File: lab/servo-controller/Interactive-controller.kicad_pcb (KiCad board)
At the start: 2 copper layers, 90 x 80 mm, 6 parts, among them U1 atmega328p

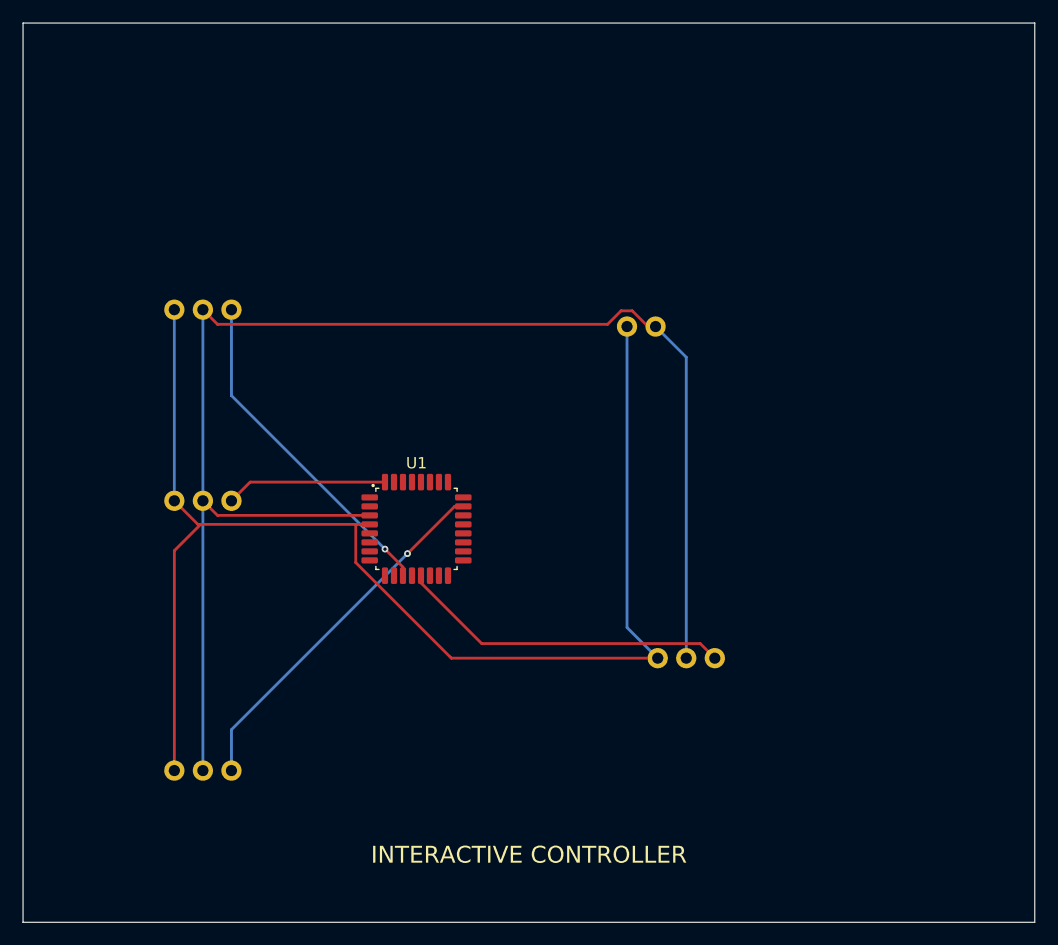
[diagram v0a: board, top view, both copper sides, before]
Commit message: lab: every board is a real board: an Arduino Nano and registry parts, routed, ready to order
The lab boards ran on simulation-only envelopes (labMcu, labDisplay, a battery). Now each is
an Arduino Nano on two sockets on the back (flashed over its USB, the image the app builds),
its lights LEDs through 1 kΩ, its knobs PTV09A pots, its display the MAX7219 eight-digit
module, its sensors an SHT31 and an SCD40 with their datasheets' support circuits, the FTDI
header for the serial console; the servo boards take 5 V on a screw terminal with a bulk
capacitor. All ten check complete with no errors or warnings, their firmware unchanged
(serial-device now on the 328P), and run in the lab without a fault (3 s each, dev host).

The registry: every interactive board must be ready to order and flash (publish.mjs refuses
one that is not; status simulation-only removed).

Claude-Session: https://claude.ai/code/session_01ATmMmxyrWxFwR3nTdXUrcx
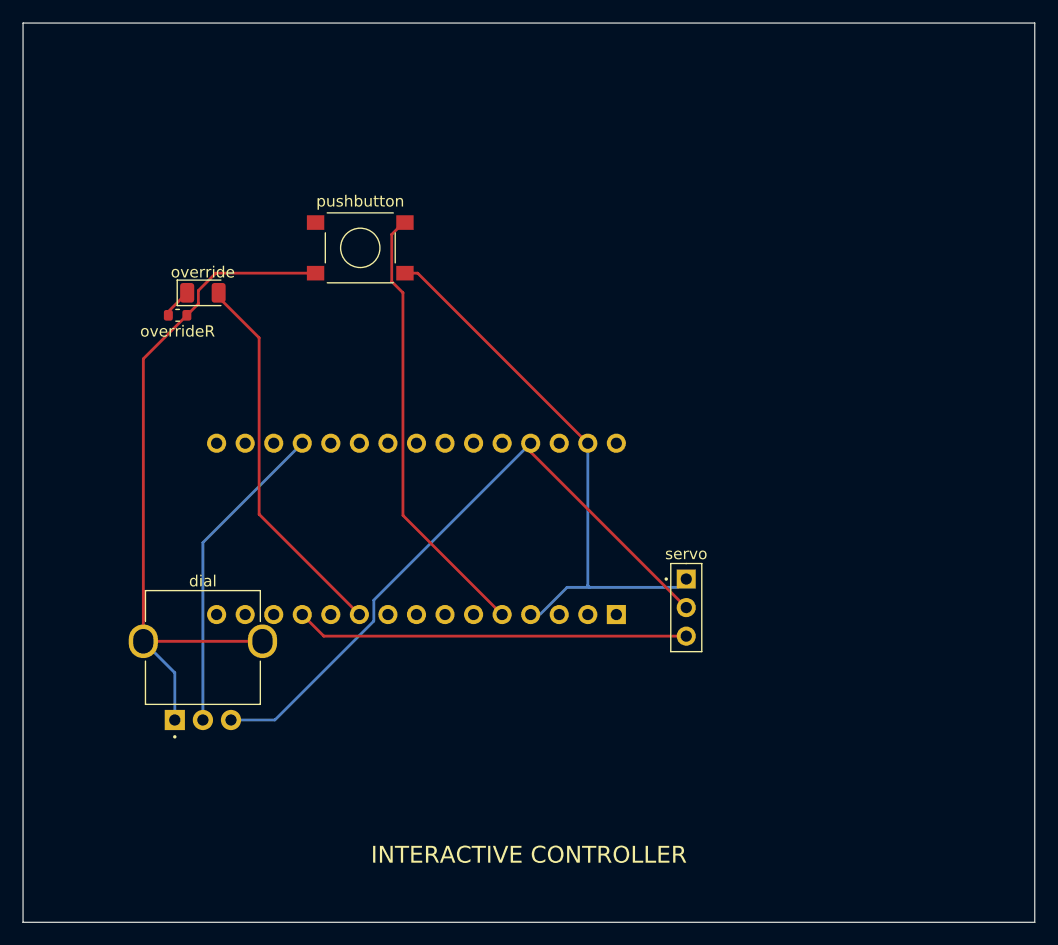
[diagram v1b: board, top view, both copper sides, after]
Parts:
- removed battery: battery, Regulated battery module
- removed button: button, Button module
- removed knob: potentiometer, Potentiometer module
- removed the override at (116.0, 144.0)
- removed the servo at (159.0, 172.0)
- added dial: PTV09A-4020F-B103, Potentiometer_Bourns_PTV09A-4_Vertical, F.Cu at (116.0, 182.0)
- added override: green, LED_1206_3216Metric, F.Cu at (116.0, 144.0)
- added overrideR: 1kohm, R_0603_1608Metric, F.Cu at (113.8, 146.0)
- added pushbutton: PTS645SM43SMTR92 LFS, SW_Tactile_SPST_6x6mm_SMD, F.Cu at (130.0, 140.0)
- added servo: RC servo header, 1 x 3 pins, 2.54 mm, PinHeader_1x03_P2.54mm_Vertical, F.Cu at (159.0, 172.0)
- U1: value atmega328p -> A000005; footprint TQFP-32_7x7mm_P0.8mm -> Arduino_Nano_Socket_2x15_P2.54mm_W15.24mm; moved to B.Cu
- turned U1 to 90 degrees
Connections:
- U1 pad 10: (no net) -> OVERRIDE
- U1 pad 11: OVERRIDE -> (no net)
- U1 pad 12: (no net) -> SERVO
- U1 pad 13: SERVO -> (no net)
- U1 pad 19: (no net) -> ANALOG
- U1 pad 23: ANALOG -> (no net)
- U1 pad 27: (no net) -> V5
- U1 pad 29: (no net) -> GND
- U1 pad 3: GND -> (no net)
- U1 pad 4: V5 -> GND
- U1 pad 5: (no net) -> BUTTON
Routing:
- net V5: track 122.5 -> 58.3 mm
- net BUTTON: track 14.3 -> 39.5 mm
- net GND: track 128.9 -> 111.7 mm
- net SERVO: track 29.6 -> 35.0 mm
- net ANALOG: track 32.5 -> 28.3 mm, vias 1 -> 0
- net OVERRIDE: track 30.0 -> 33.8 mm, vias 1 -> 0
- net OVERRIDE_K: track 0.00 -> 2.69 mm

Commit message: Boards pass check and KiCad 10's DRC again: holes in courtyards, the USB net rename
pcbkit's check now has KiCad 10's pth/npth_inside_courtyard (pcbkit be5b6955), and 13 boards
failed it. KiCad's own DRC (kicad-cli 10) reports the same holes on every one of them.

- Parts that really stand above the holes under them (a screen or a Nano on its sockets, the
  Delta-S02's КМ-6 capacitors flat under its chips, as the factory placed them): a courtyard rule
  for the pair, written to each board's .kicad_dru, so KiCad's DRC agrees.
- Real collisions moved: servo-controller's dial 3 mm up (the Nano's socket pins came out under
  it), c3-pocket's fourth M3 hole from under a cell holder to the top edge's middle, s3-rgb's
  D-pad 2 mm up (a holder's peg came through under the down key).
- v003-emu, c3-pocket, rp2040-tft, rp2350-psram, s3-rgb, teensy41: re-routed for the standard USB
  block's renamed net (usb/raw is usb/vbusIn since pcbkit 2088839e): their tracks still carried
  the old name and shorted the fuse and connector pads.
- p4-touch-7: its board file still had a courtyard for the panel the design gives none (KiCad
  reported 114 courtyard errors); written again.

Measured on the dev host: all 44 registry boards `pcbkit check` complete with 0 errors, and
kicad-cli pcb drc 0 errors on every board.

Claude-Session: https://claude.ai/code/session_018URVYF1YPgyrMNetY9yT1T
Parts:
- moved dial 3.00 mm to (116.0, 185.0)
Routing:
- net ANALOG: track 28.3 -> 31.3 mm
- net V5: track 58.3 -> 59.5 mm

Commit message: lab, examples, esp32-p4-touch-lcd-7b: the sweep's errors and stale parts
- lab/stopwatch: the display module stands on its socket above the Nano's socket pins. It now has
  the courtyard waiver the other Nano boards have (13 pth-inside-courtyard -> 0).
- lab/servo-controller: outline 90 x 80 -> 70 x 70 mm, with the parts where they were
  (board-oversized, plan-size: 11 % parts). Complete, 0 warnings.
- examples/blinker, examples/led-bar, devices/esp32-p4-touch-lcd-7b: `pcbkit parts` chose again
  where the recorded part no longer met the need (part-stale).

Claude-Session: https://claude.ai/code/session_01B3VRfBCg9vAvGVWujVGarr
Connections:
- pushbutton pad 2: BUTTON -> GND
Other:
- board size 90 x 80 mm -> 70 x 70 mm
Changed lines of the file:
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@@
   (footprint "Arduino_Nano_Socket_2x15_P2.54mm_W15.24mm" (layer "B.Cu") (at 135 165 90)
     (descr "Arduino Nano on two 1x15 female headers 15.24 mm apart, its USB end at +Y (Arduino's drawing): pins 1-15 the right row from the bottom (D1/TX … D12), 16-30 the left row from the top (D13 … VIN)")
-    (tags "THT module pin socket female header")
+    (tags "THT module pin header soldered")
     (property "Reference" "U1" (at 0 -24.05 90) (layer "B.SilkS") (effects (font (size 1 1) (thickness 0.15)) (justify mirror)))
     (property "Value" "A000005" (at 0 0 0) (layer "B.Fab") (hide yes) (effects (font (size 1 1))))
@@
     (property "Status" "checked" (at 0 0 0) (layer "B.Fab") (hide yes) (effects (font (size 1 1))))
     (property "pcbkit" "U1" (at 0 0 0) (layer "B.Fab") (hide yes) (effects (font (size 1 1))))
-    (fp_rect (start 9.25 21.85) (end -9.25 -23.35) (stroke (width 0.05) (type solid)) (layer "B.CrtYd"))
+    (fp_poly (pts (xy -6.12 19.28) (xy -9.12 19.28) (xy -9.12 16.28) (xy -6.12 16.28)) (stroke (width 0.05) (type solid)) (fill none) (layer "B.CrtYd"))
+    (fp_poly (pts (xy -6.12 16.74) (xy -9.12 16.74) (xy -9.12 13.74) (xy -6.12 13.74)) (stroke (width 0.05) (type solid)) (fill none) (layer "B.CrtYd"))
+    (fp_poly (pts (xy -6.12 14.2) (xy -9.12 14.2) (xy -9.12 11.2) (xy -6.12 11.2)) (stroke (width 0.05) (type solid)) (fill none) (layer "B.CrtYd"))
+    (fp_poly (pts (xy -6.12 11.66) (xy -9.12 11.66) (xy -9.12 8.66) (xy -6.12 8.66)) (stroke (width 0.05) (type solid)) (fill none) (layer "B.CrtYd"))
+    (fp_poly (pts (xy -6.12 9.12) (xy -9.12 9.12) (xy -9.12 6.12) (xy -6.12 6.12)) (stroke (width 0.05) (type solid)) (fill none) (layer "B.CrtYd"))
+    (fp_poly (pts (xy -6.12 6.58) (xy -9.12 6.58) (xy -9.12 3.58) (xy -6.12 3.58)) (stroke (width 0.05) (type solid)) (fill none) (layer "B.CrtYd"))
+    (fp_poly (pts (xy -6.12 4.04) (xy -9.12 4.04) (xy -9.12 1.04) (xy -6.12 1.04)) (stroke (width 0.05) (type solid)) (fill none) (layer "B.CrtYd"))
+    (fp_poly (pts (xy -6.12 1.5) (xy -9.12 1.5) (xy -9.12 -1.5) (xy -6.12 -1.5)) (stroke (width 0.05) (type solid)) (fill none) (layer "B.CrtYd"))
+    (fp_poly (pts (xy -6.12 -1.04) (xy -9.12 -1.04) (xy -9.12 -4.04) (xy -6.12 -4.04)) (stroke (width 0.05) (type solid)) (fill none) (layer "B.CrtYd"))
+    (fp_poly (pts (xy -6.12 -3.58) (xy -9.12 -3.58) (xy -9.12 -6.58) (xy -6.12 -6.58)) (stroke (width 0.05) (type solid)) (fill none) (layer "B.CrtYd"))
+    (fp_poly (pts (xy -6.12 -6.12) (xy -9.12 -6.12) (xy -9.12 -9.12) (xy -6.12 -9.12)) (stroke (width 0.05) (type solid)) (fill none) (layer "B.CrtYd"))
+    (fp_poly (pts (xy -6.12 -8.66) (xy -9.12 -8.66) (xy -9.12 -11.66) (xy -6.12 -11.66)) (stroke (width 0.05) (type solid)) (fill none) (layer "B.CrtYd"))
+    (fp_poly (pts (xy -6.12 -11.2) (xy -9.12 -11.2) (xy -9.12 -14.2) (xy -6.12 -14.2)) (stroke (width 0.05) (type solid)) (fill none) (layer "B.CrtYd"))
+    (fp_poly (pts (xy -6.12 -13.74) (xy -9.12 -13.74) (xy -9.12 -16.74) (xy -6.12 -16.74)) (stroke (width 0.05) (type solid)) (fill none) (layer "B.CrtYd"))
+    (fp_poly (pts (xy -6.12 -16.28) (xy -9.12 -16.28) (xy -9.12 -19.28) (xy -6.12 -19.28)) (stroke (width 0.05) (type solid)) (fill none) (layer "B.CrtYd"))
+    (fp_poly (pts (xy 9.12 -16.28) (xy 6.12 -16.28) (xy 6.12 -19.28) (xy 9.12 -19.28)) (stroke (width 0.05) (type solid)) (fill none) (layer "B.CrtYd"))
+    (fp_poly (pts (xy 9.12 -13.74) (xy 6.12 -13.74) (xy 6.12 -16.74) (xy 9.12 -16.74)) (stroke (width 0.05) (type solid)) (fill none) (layer "B.CrtYd"))
+    (fp_poly (pts (xy 9.12 -11.2) (xy 6.12 -11.2) (xy 6.12 -14.2) (xy 9.12 -14.2)) (stroke (width 0.05) (type solid)) (fill none) (layer "B.CrtYd"))
+    (fp_poly (pts (xy 9.12 -8.66) (xy 6.12 -8.66) (xy 6.12 -11.66) (xy 9.12 -11.66)) (stroke (width 0.05) (type solid)) (fill none) (layer "B.CrtYd"))
+    (fp_poly (pts (xy 9.12 -6.12) (xy 6.12 -6.12) (xy 6.12 -9.12) (xy 9.12 -9.12)) (stroke (width 0.05) (type solid)) (fill none) (layer "B.CrtYd"))
+    (fp_poly (pts (xy 9.12 -3.58) (xy 6.12 -3.58) (xy 6.12 -6.58) (xy 9.12 -6.58)) (stroke (width 0.05) (type solid)) (fill none) (layer "B.CrtYd"))
+    (fp_poly (pts (xy 9.12 -1.04) (xy 6.12 -1.04) (xy 6.12 -4.04) (xy 9.12 -4.04)) (stroke (width 0.05) (type solid)) (fill none) (layer "B.CrtYd"))
+    (fp_poly (pts (xy 9.12 1.5) (xy 6.12 1.5) (xy 6.12 -1.5) (xy 9.12 -1.5)) (stroke (width 0.05) (type solid)) (fill none) (layer "B.CrtYd"))
+    (fp_poly (pts (xy 9.12 4.04) (xy 6.12 4.04) (xy 6.12 1.04) (xy 9.12 1.04)) (stroke (width 0.05) (type solid)) (fill none) (layer "B.CrtYd"))
+    (fp_poly (pts (xy 9.12 6.58) (xy 6.12 6.58) (xy 6.12 3.58) (xy 9.12 3.58)) (stroke (width 0.05) (type solid)) (fill none) (layer "B.CrtYd"))
+    (fp_poly (pts (xy 9.12 9.12) (xy 6.12 9.12) (xy 6.12 6.12) (xy 9.12 6.12)) (stroke (width 0.05) (type solid)) (fill none) (layer "B.CrtYd"))
+    (fp_poly (pts (xy 9.12 11.66) (xy 6.12 11.66) (xy 6.12 8.66) (xy 9.12 8.66)) (stroke (width 0.05) (type solid)) (fill none) (layer "B.CrtYd"))
+    (fp_poly (pts (xy 9.12 14.2) (xy 6.12 14.2) (xy 6.12 11.2) (xy 9.12 11.2)) (stroke (width 0.05) (type solid)) (fill none) (layer "B.CrtYd"))
+    (fp_poly (pts (xy 9.12 16.74) (xy 6.12 16.74) (xy 6.12 13.74) (xy 9.12 13.74)) (stroke (width 0.05) (type solid)) (fill none) (layer "B.CrtYd"))
+    (fp_poly (pts (xy 9.12 19.28) (xy 6.12 19.28) (xy 6.12 16.28) (xy 9.12 16.28)) (stroke (width 0.05) (type solid)) (fill none) (layer "B.CrtYd"))
+    (fp_poly (pts (xy 6.2 17.29) (xy -5.515 17.29) (xy -5.515 -10.35) (xy 6.2 -10.35)) (stroke (width 0.05) (type solid)) (fill none) (layer "B.CrtYd"))
     (fp_line (start 0 -23.21) (end 9.11 -23.21) (stroke (width 0.12) (type solid)) (layer "B.SilkS"))
     (fp_line (start 9.11 -23.21) (end 9.11 21.71) (stroke (width 0.12) (type solid)) (layer "B.SilkS"))
@@
   )
   (footprint "SW_Tactile_SPST_6x6mm_SMD" (layer "F.Cu") (at 130 140 0)
-    (descr "Tactile switch, 6 x 6 x 4.3 mm, SMD, 4 pads (1-2 and 3-4 joined)")
+    (descr "Tactile switch, 6 x 6 x 4.3 mm, SMD, 4 pads, 2 to each contact")
     (tags "switch tactile button 6x6")
     (property "Reference" "pushbutton" (at 0 -4.141667 0) (layer "F.SilkS") (effects (font (size 1 1) (thickness 0.15))))
@@
     (property "Manufacturer" "C&K" (at 0 0 0) (layer "F.Fab") (hide yes) (effects (font (size 1 1))))
     (property "pcbkit" "pushbutton" (at 0 0 0) (layer "F.Fab") (hide yes) (effects (font (size 1 1))))
-    (jumper_pad_groups ("1" "2") ("3" "4"))
+    (duplicate_pad_numbers_are_jumpers yes)
     (fp_rect (start -5 3.25) (end 5 -3.25) (stroke (width 0.05) (type solid)) (layer "F.CrtYd"))
     (fp_line (start -3.11 -1.34) (end -3.11 1.34) (stroke (width 0.12) (type solid)) (layer "F.SilkS"))
@@
     (fp_circle (center 0 0) (end 1.75 0) (stroke (width 0.12) (type solid)) (fill none) (layer "F.SilkS"))
     (pad "1" smd rect (at -3.975 -2.25 0) (size 1.55 1.3) (layers "F.Cu" "F.Paste" "F.Mask") (solder_mask_margin 0.05) (net 2 "BUTTON"))
-    (pad "2" smd rect (at 3.975 -2.25 0) (size 1.55 1.3) (layers "F.Cu" "F.Paste" "F.Mask") (solder_mask_margin 0.05) (net 2 "BUTTON"))
-    (pad "3" smd rect (at -3.975 2.25 0) (size 1.55 1.3) (layers "F.Cu" "F.Paste" "F.Mask") (solder_mask_margin 0.05) (net 3 "GND"))
-    (pad "4" smd rect (at 3.975 2.25 0) (size 1.55 1.3) (layers "F.Cu" "F.Paste" "F.Mask") (solder_mask_margin 0.05) (net 3 "GND"))
+    (pad "1" smd rect (at 3.975 -2.25 0) (size 1.55 1.3) (layers "F.Cu" "F.Paste" "F.Mask") (solder_mask_margin 0.05) (net 2 "BUTTON"))
+    (pad "2" smd rect (at -3.975 2.25 0) (size 1.55 1.3) (layers "F.Cu" "F.Paste" "F.Mask") (solder_mask_margin 0.05) (net 3 "GND"))
+    (pad "2" smd rect (at 3.975 2.25 0) (size 1.55 1.3) (layers "F.Cu" "F.Paste" "F.Mask") (solder_mask_margin 0.05) (net 3 "GND"))
   )
   (footprint "PinHeader_1x03_P2.54mm_Vertical" (layer "F.Cu") (at 159 172 0)
@@
     (pad "3" thru_hole oval (at 0 2.54 0) (size 1.7 1.7) (drill 1) (layers "*.Cu" "*.Mask") (solder_mask_margin 0.05) (net 6 "SERVO"))
   )
-  (gr_text "INTERACTIVE CONTROLLER" (at 145 194 0) (layer "F.SilkS") (effects (font (size 1.5 1.5) (thickness 0.15))))
-  (group "pcbkit" (members "e2fbeeec-4a09-db61-f9d1-26c3135e6155"))
   (segment (start 114.6 144) (end 112.925 145.675) (width 0.25) (layer "F.Cu") (net 5))
   (segment (start 112.925 145.675) (end 112.925 146) (width 0.25) (layer "F.Cu") (net 5))
@@
   (segment (start 133.85 137.75) (end 133.975 137.75) (width 0.25) (layer "F.Cu") (net 2))
   (segment (start 121.3 178) (end 110.7 178) (width 0.25) (layer "F.Cu") (net 3))
-  (gr_line (start 100 200) (end 190 200) (stroke (width 0.1) (type solid)) (layer "Edge.Cuts"))
-  (gr_line (start 190 200) (end 190 120) (stroke (width 0.1) (type solid)) (layer "Edge.Cuts"))
-  (gr_line (start 190 120) (end 100 120) (stroke (width 0.1) (type solid)) (layer "Edge.Cuts"))
-  (gr_line (start 100 120) (end 100 200) (stroke (width 0.1) (type solid)) (layer "Edge.Cuts"))
   (segment (start 145.16 157.38) (end 145.16 158.16) (width 0.25) (layer "F.Cu") (net 7))
   (segment (start 145.16 158.16) (end 159 172) (width 0.25) (layer "F.Cu") (net 7))
@@
   (segment (start 110.7 178) (end 113.5 180.8) (width 0.25) (layer "B.Cu") (net 3))
   (segment (start 113.5 180.8) (end 113.5 185) (width 0.25) (layer "B.Cu") (net 3))
+  (gr_text "INTERACTIVE CONTROLLER" (at 135 195 0) (layer "F.SilkS") (effects (font (size 1.5 1.5) (thickness 0.15))))
+  (group "pcbkit" (members "4508d8a0-57a5-5a2e-1e66-5559b5bddc9e"))
+  (gr_line (start 100 200) (end 170 200) (stroke (width 0.1) (type solid)) (layer "Edge.Cuts"))
+  (gr_line (start 170 200) (end 170 130) (stroke (width 0.1) (type solid)) (layer "Edge.Cuts"))
+  (gr_line (start 170 130) (end 100 130) (stroke (width 0.1) (type solid)) (layer "Edge.Cuts"))
+  (gr_line (start 100 130) (end 100 200) (stroke (width 0.1) (type solid)) (layer "Edge.Cuts"))
 )
